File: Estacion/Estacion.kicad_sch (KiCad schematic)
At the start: 8 parts, among them U1 FN-M16P, U2 RP2040-ZERO, U3 DHT22

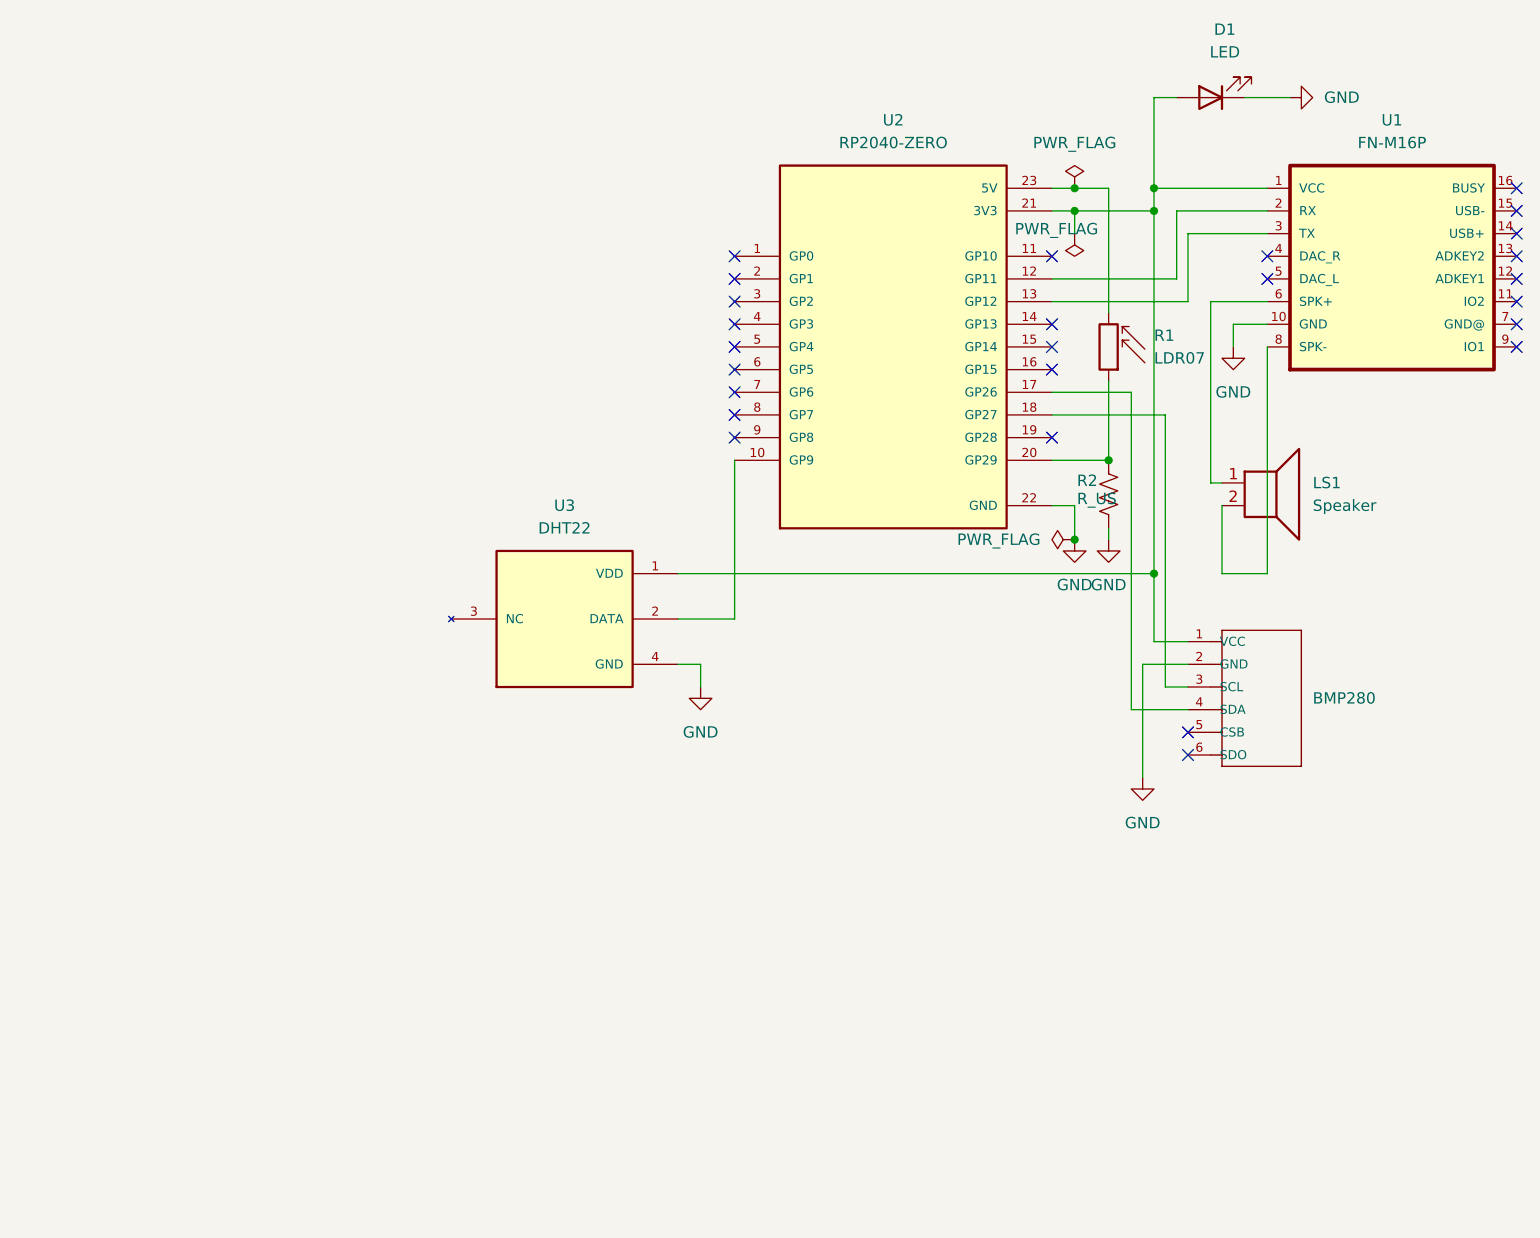
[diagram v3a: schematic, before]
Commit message: Wemos s2 mini
Se cambia el controlador y se realizan las conexiones en el diagrama
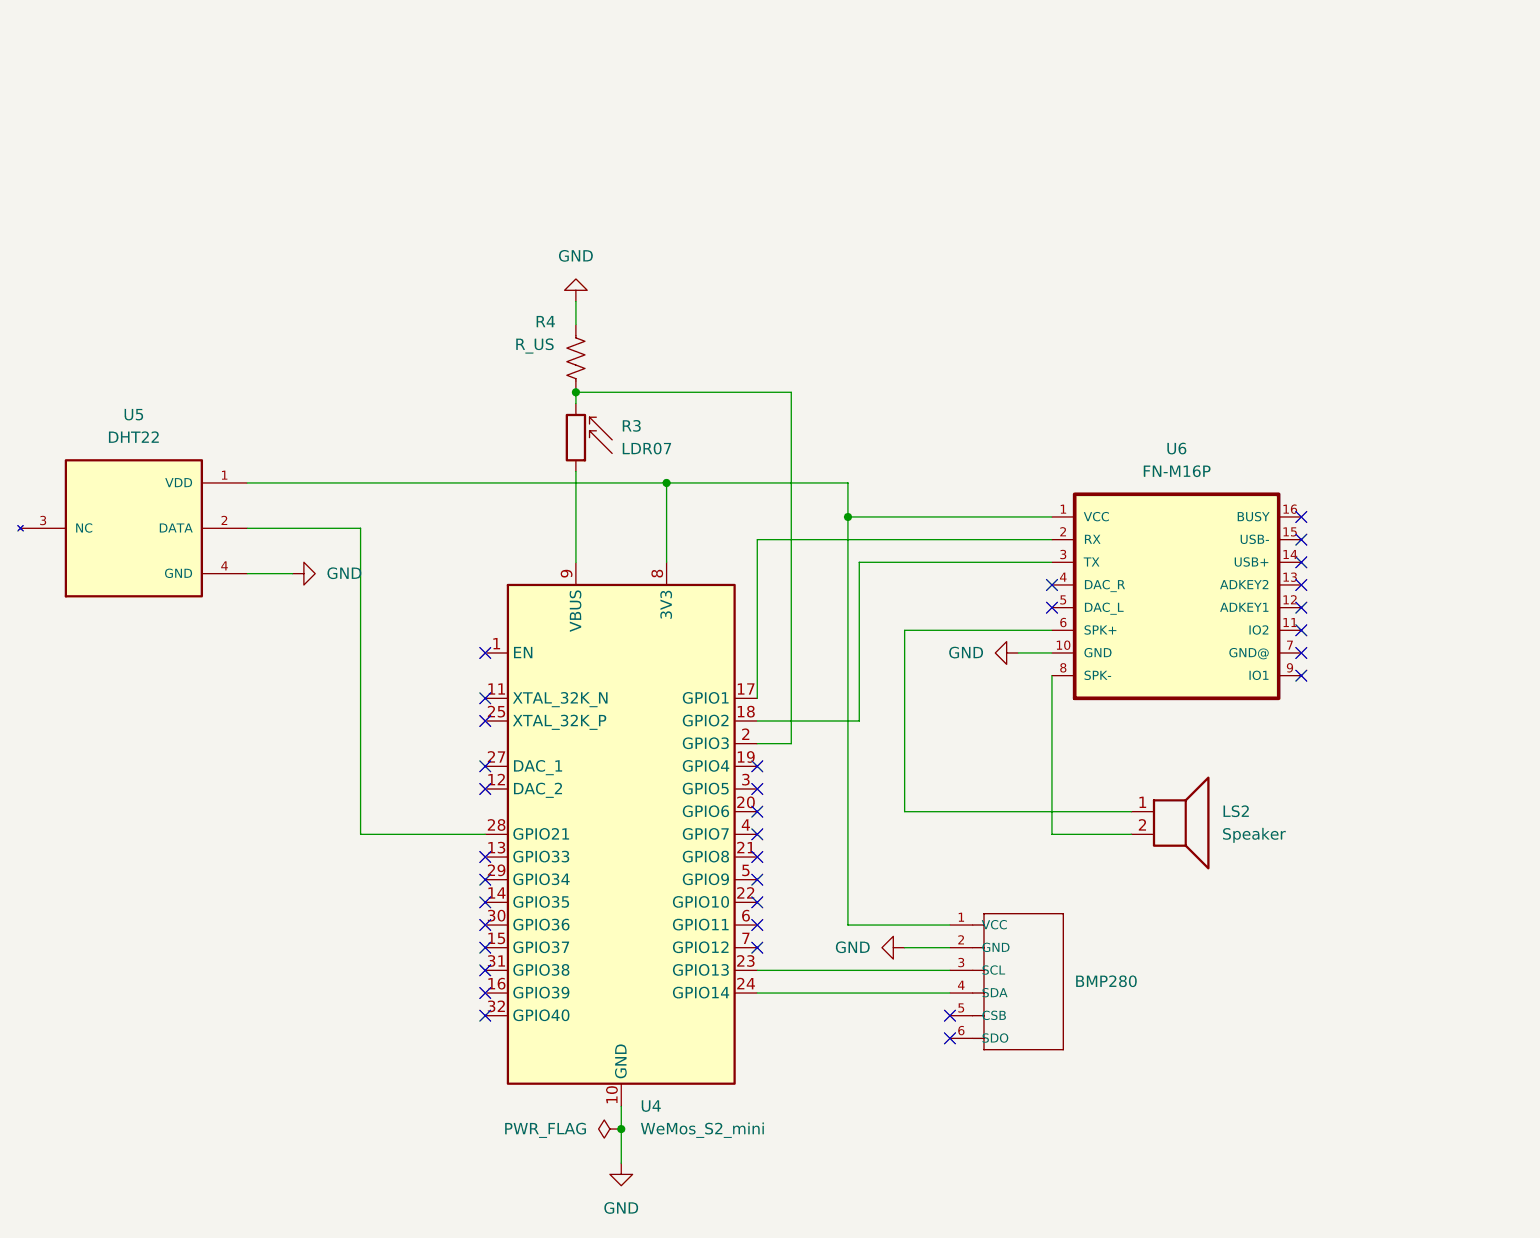
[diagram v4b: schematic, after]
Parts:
- removed D1: LED, symbol Device:LED
- removed LS1: Speaker, symbol Device:Speaker
- removed R1: LDR07, OptoDevice:R_LDR_5.1x4.3mm_P3.4mm_Vertical, symbol Sensor_Optical:LDR07
- removed R2: R_US, Resistor_THT:R_Axial_DIN0204_L3.6mm_D1.6mm_P5.08mm_Horizontal, symbol Device:R_US
- removed U1: FN-M16P, especificos:FN-M16P, symbol FDPlayer:FN-M16P
- removed U2: RP2040-ZERO, especificos:MODULE_RP2040-ZERO, symbol PICO ZERO:RP2040-ZERO
- removed U3: DHT22, especificos:XDCR_DHT22, symbol DHT22:DHT22
- added LS2: Speaker, symbol Device:Speaker
- added R3: LDR07, OptoDevice:R_LDR_5.1x4.3mm_P3.4mm_Vertical, symbol Sensor_Optical:LDR07
- added R4: R_US, Resistor_THT:R_Axial_DIN0204_L3.6mm_D1.6mm_P5.08mm_Horizontal, symbol Device:R_US
- added U4: WeMos_S2_mini, especificos:WEMOS_S2_mini, symbol prueba:WeMos_S2_mini
- added U5: DHT22, especificos:XDCR_DHT22, symbol DHT22:DHT22
- added U6: FN-M16P, especificos:FN-M16P, symbol FDPlayer:FN-M16P
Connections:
- net GND: now also R4.1, U4.10 (GND), U4.26 (GND), U5.4 (GND), U6.10 (GND)
- net at BMP280.1 (VCC): now also U4.8 (3V3), U5.1 (VDD), U6.1 (VCC)
- net at BMP280.4 (SDA): now also U4.24 (GPIO14)
- net at BMP280.3 (SCL): now also U4.23 (GPIO13)
- new net: U4.17 (GPIO1), U6.2 (RX)
- new net: U4.18 (GPIO2), U6.3 (TX)
- new net: R3.2, R4.2, U4.2 (GPIO3)
- new net: U4.28 (GPIO21), U5.2 (DATA)
- new net: R3.1, U4.9 (VBUS)
- new net: LS2.1, U6.6 (SPK+)
- new net: LS2.2, U6.8 (SPK-)
- no-connect marks 26 -> 34

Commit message: .
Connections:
- net at U4.16 (GPIO39): now also R3.2, R4.2
- now unconnected: U4.2 (GPIO3)
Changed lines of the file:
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@@
 	(paper "A4")
 	(junction
+		(at 114.3 140.97)
+		(diameter 0)
+		(color 0 0 0 0)
+	)
+	(junction
+		(at 119.38 68.58)
+		(diameter 0)
+		(color 0 0 0 0)
+	)
+	(junction
+		(at 139.7 72.39)
+		(diameter 0)
+		(color 0 0 0 0)
+	)
+	(junction
 		(at 109.22 58.42)
 		(diameter 0)
 		(color 0 0 0 0)
 	)
-	(junction
-		(at 114.3 140.97)
-		(diameter 0)
-		(color 0 0 0 0)
-	)
-	(junction
-		(at 119.38 68.58)
-		(diameter 0)
-		(color 0 0 0 0)
-	)
-	(junction
-		(at 139.7 72.39)
-		(diameter 0)
-		(color 0 0 0 0)
-	)
 	(no_connect
 		(at 99.06 92.71)
@@
 	)
 	(no_connect
-		(at 99.06 125.73)
-	)
-	(no_connect
 		(at 99.06 95.25)
 	)
@@
 	)
 	(no_connect
+		(at 129.54 97.79)
+	)
+	(no_connect
 		(at 99.06 102.87)
 	)
@@
 	(wire
 		(pts
-			(xy 109.22 58.42) (xy 133.35 58.42)
+			(xy 109.22 58.42) (xy 90.17 58.42)
 		)
 		(stroke
@@
 	(wire
 		(pts
+			(xy 90.17 125.73) (xy 99.06 125.73)
+		)
+		(stroke
+			(width 0)
+			(type default)
+		)
+	)
+	(wire
+		(pts
 			(xy 72.39 68.58) (xy 119.38 68.58)
 		)
@@
 	(wire
 		(pts
+			(xy 90.17 58.42) (xy 90.17 125.73)
+		)
+		(stroke
+			(width 0)
+			(type default)
+		)
+	)
+	(wire
+		(pts
 			(xy 129.54 125.73) (xy 151.13 125.73)
 		)
@@
 	(wire
 		(pts
-			(xy 133.35 58.42) (xy 133.35 97.79)
-		)
-		(stroke
-			(width 0)
-			(type default)
-		)
-	)
-	(wire
-		(pts
 			(xy 109.22 58.42) (xy 109.22 59.69)
 		)
@@
 		)
 		(stroke
-			(width 0)
-			(type default)
-		)
-	)
-	(wire
-		(pts
-			(xy 133.35 97.79) (xy 129.54 97.79)
-		)
-		(stroke

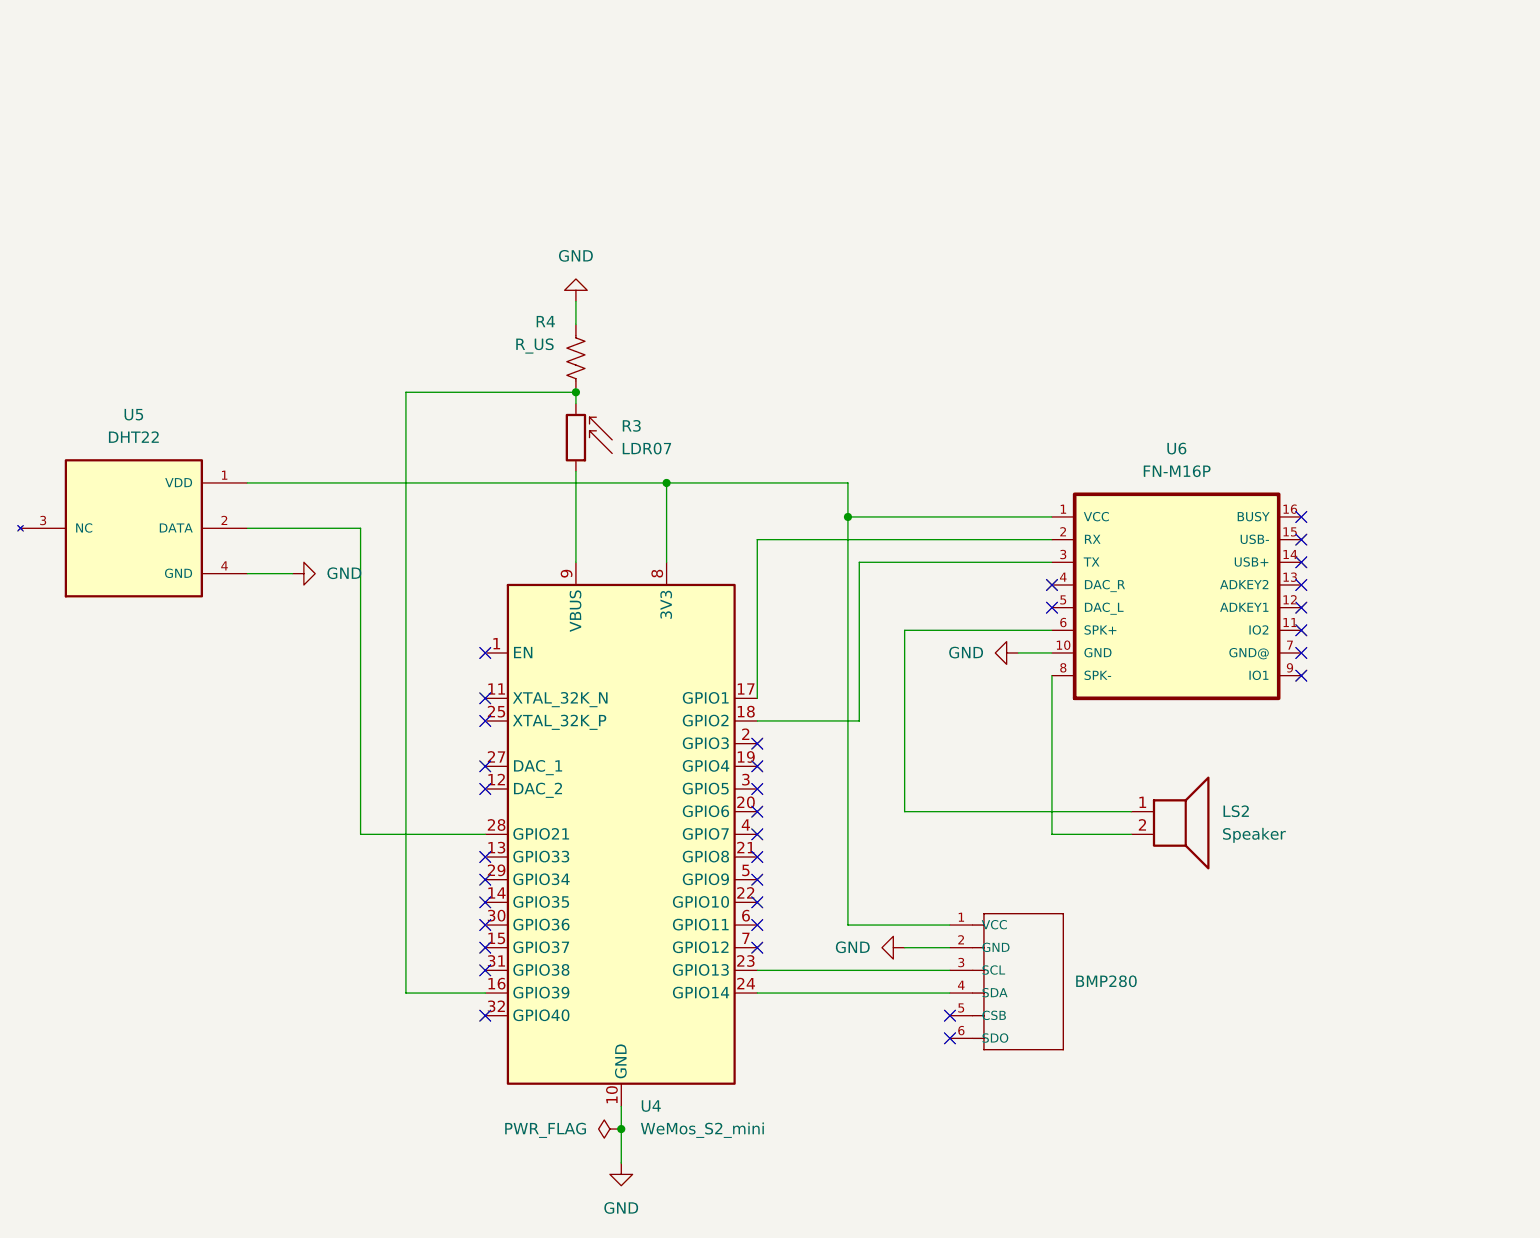
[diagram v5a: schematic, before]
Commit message: Girar los GND para que apunten abajo y agregar la net 3v3
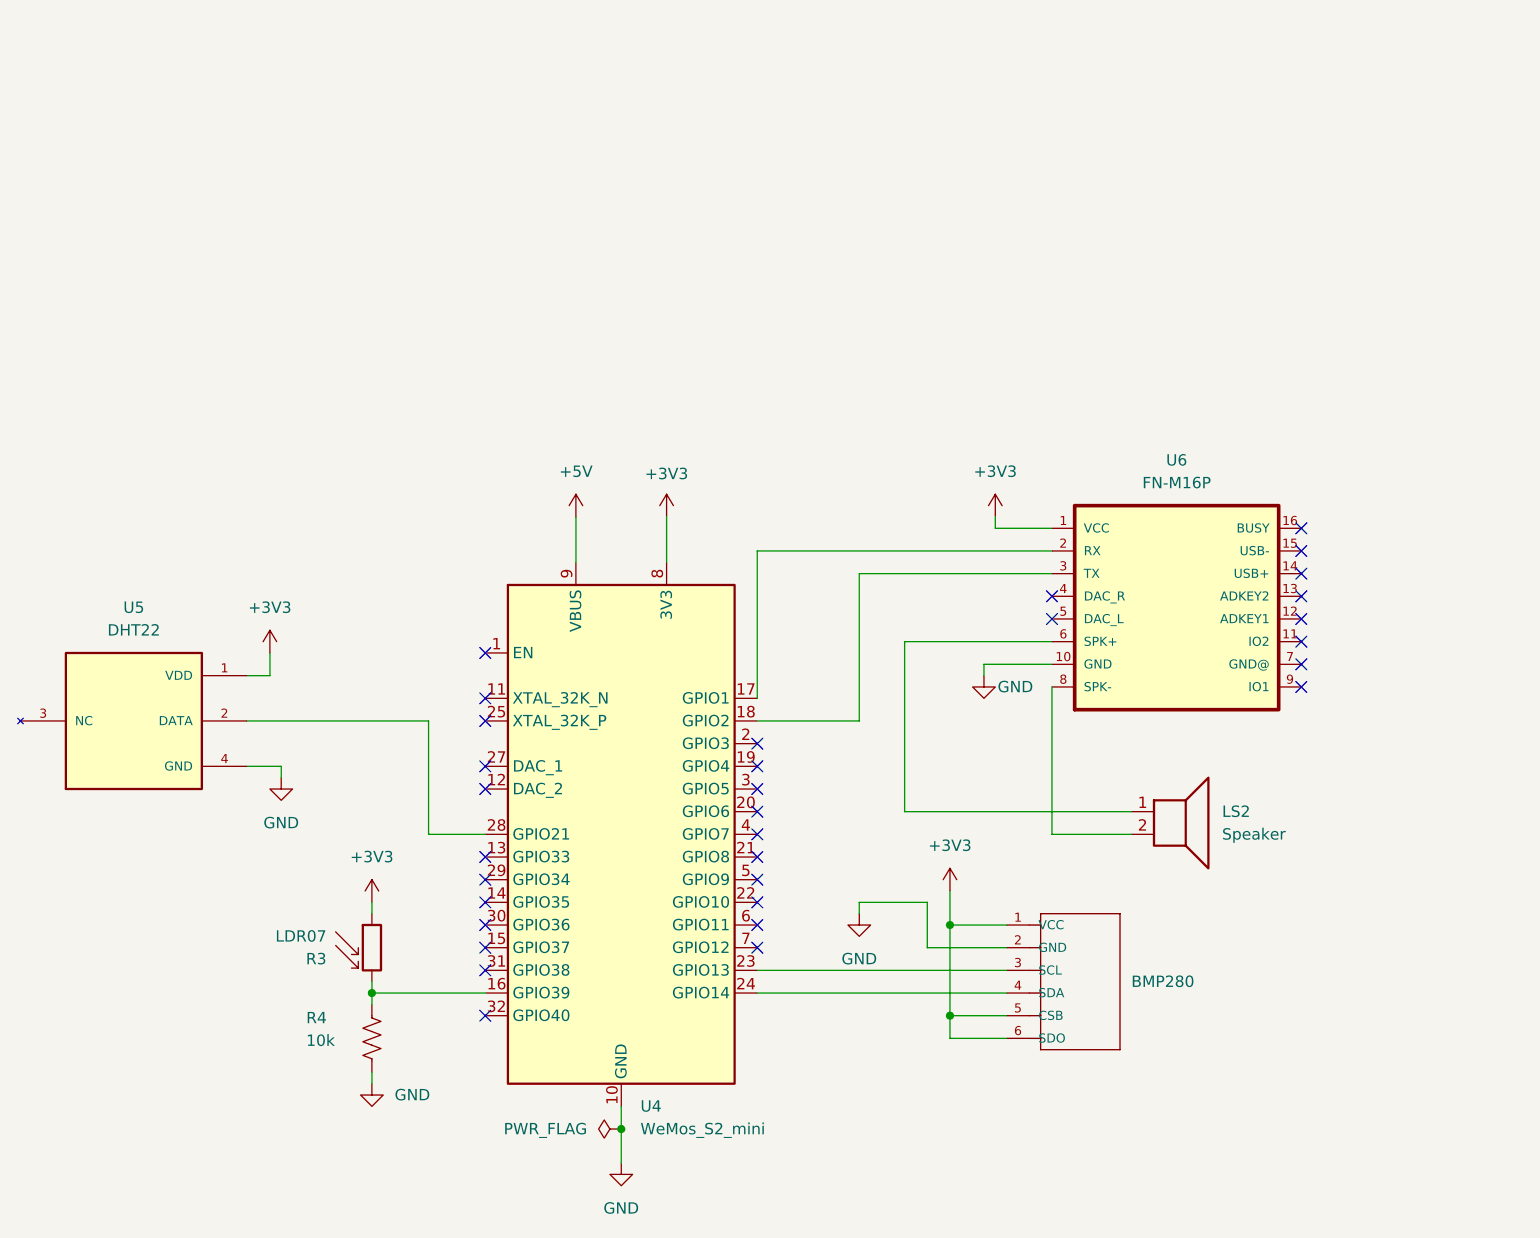
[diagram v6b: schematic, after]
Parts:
- R4: value R_US -> 10k
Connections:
- net GND: now also R4.2; no longer R4.1
- net at R3.2, U4.16 (GPIO39): now also R4.1; no longer R4.2
- net +3V3: now reaches BMP280.1 (VCC), U4.8 (3V3), U5.1 (VDD), U6.1 (VCC)
- net +3V3: now also BMP280.5 (CSB), BMP280.6 (SDO), R3.1
- net +5V: now reaches U4.9 (VBUS)
- net +5V: no longer R3.1
- no-connect marks 34 -> 32
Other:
- moved on the sheet: BMP280, R3, R4, U5, U6
